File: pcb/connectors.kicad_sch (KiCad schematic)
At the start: 2 parts, among them J1 OBD2, J2 CAN

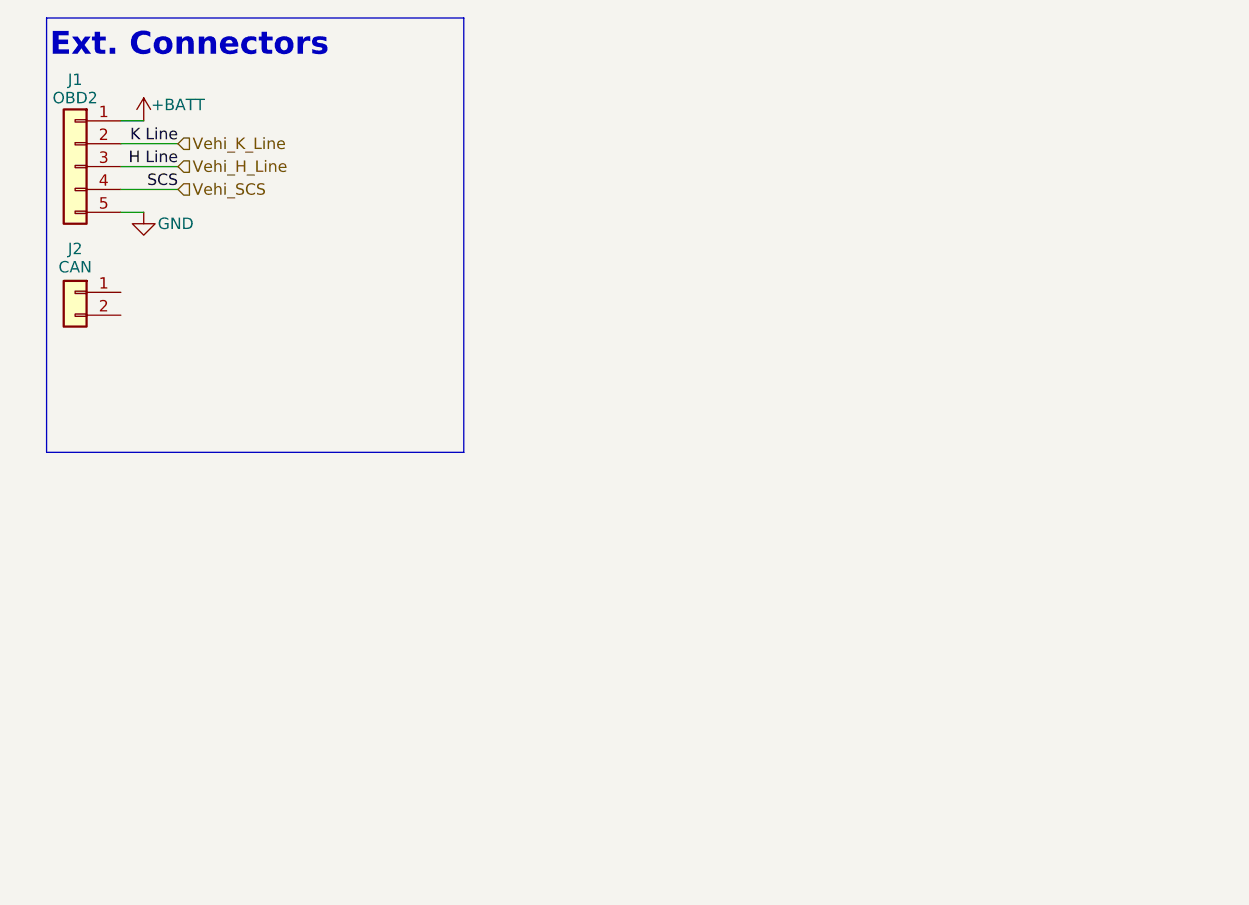
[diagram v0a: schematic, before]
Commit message: add transceivers, routing, drc
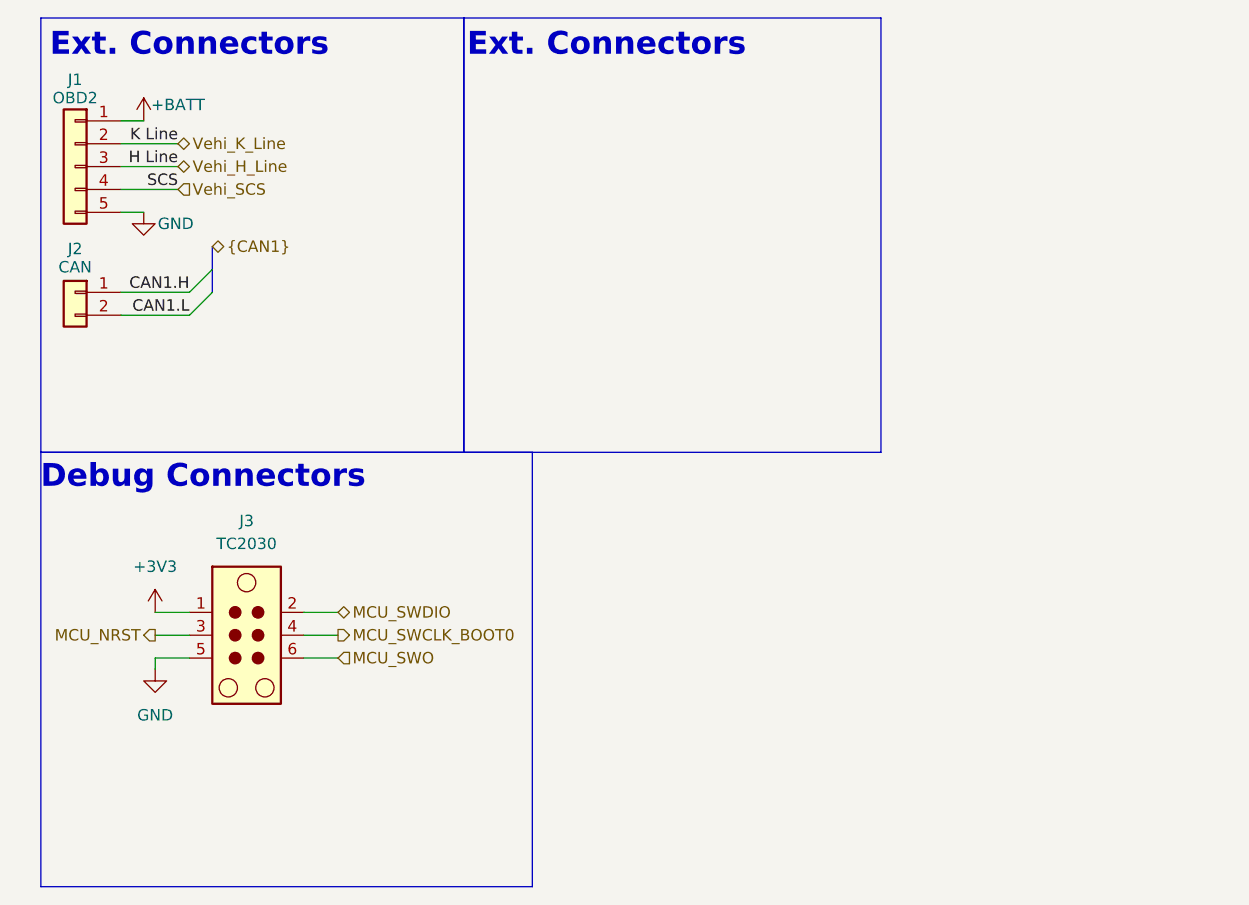
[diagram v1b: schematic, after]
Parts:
- added J3: TC2030, Connector:Tag-Connect_TC2030-IDC-NL_2x03_P1.27mm_Vertical, symbol Connector:TC2030
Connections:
- net GND: now also J3.5
- net CAN1.H: now reaches J2.1 (Pin_1)
- net CAN1.L: now reaches J2.2 (Pin_2)
- new net +3V3: J3.1
- new net MCU_NRST: J3.3
- new net MCU_SWCLK_BOOT0: J3.4
- new net MCU_SWDIO: J3.2
- new net MCU_SWO: J3.6
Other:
- note added: "Debug Connectors"

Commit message: busses are hard
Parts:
- added J3: USB-C 2.0, Connector_USB:USB_C_Receptacle_GCT_USB4105-xx-A_16P_TopMnt_Horizontal, symbol Connector:USB_C_Receptacle_USB2.0_16P
- added J4: RTC_BAT, Connector_Molex:Molex_PicoBlade_53047-0210_1x02_P1.25mm_Vertical, symbol Connector_Generic:Conn_01x02
- added R401, R402: 5.1k, Resistor_SMD:R_0402_1005Metric, symbol Device:R_Small
- renumbered J3 to J_SWD1
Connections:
- net GND: now also J3.A1 (GND), J3.A12 (GND), J3.B1 (GND), J3.B12 (GND), J3.S1 (SHIELD), J4.2 (Pin_2), R401.1, R402.2
- net CAN1.H renamed H_+
- net CAN1.L renamed L_-
- new net: J3.B5 (CC2), R402.1
- new net: J3.A5 (CC1), R401.2
- new net DN: J3.A7 (D-), J3.B7 (D-)
- new net DP: J3.A6 (D+), J3.B6 (D+)
- new net RTC_VBAT: J4.1 (Pin_1)
- new net USB_5V: J3.A4 (VBUS), J3.A9 (VBUS), J3.B4 (VBUS), J3.B9 (VBUS)
- no-connect marks 0 -> 2
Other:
- note added: "Int. Connectors"
- moved on the sheet: J1, J2, J_SWD1

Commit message: CAN/mcu placement/routing
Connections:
- net H_+ renamed CAN.P
- net L_- renamed CAN.N
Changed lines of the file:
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@@
 		)
 	)
-	(label "H_+"
+	(label "CAN.P"
 		(at 27.94 50.8 0)
 		(effects
@@
 		)
 	)
-	(label "L_-"
+	(label "CAN.N"
 		(at 27.94 53.34 0)
 		(effects
@@
 		)
 	)
-	(hierarchical_label "{CAN}"
+	(hierarchical_label "CAN{CAN}"
 		(shape bidirectional)
 		(at 36.83 45.72 180)

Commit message: fix CAN tx/rx/stb, remove unused SWO
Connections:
- net MCU_SWO: no longer names the net of J_SWD1.6
- no-connect marks 2 -> 3
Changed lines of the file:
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@@
 		(at 74.93 53.34)
+	)
+	(no_connect
+		(at 44.45 87.63)
 	)
 	(bus_entry
@@
 	(wire
 		(pts
-			(xy 44.45 87.63) (xy 48.26 87.63)
-		)
-		(stroke
-			(width 0)
-			(type default)
-		)
-	)
-	(wire
-		(pts
 			(xy 74.93 35.56) (xy 76.2 35.56)
 		)
@@
 		(effects
 			(font
-				(size 1.27 1.27)
-			)
-			(justify left)
-		)
-	)
-	(hierarchical_label "MCU_SWO"
-		(shape input)
-		(at 48.26 87.63 0)
-		(effects
-			(font

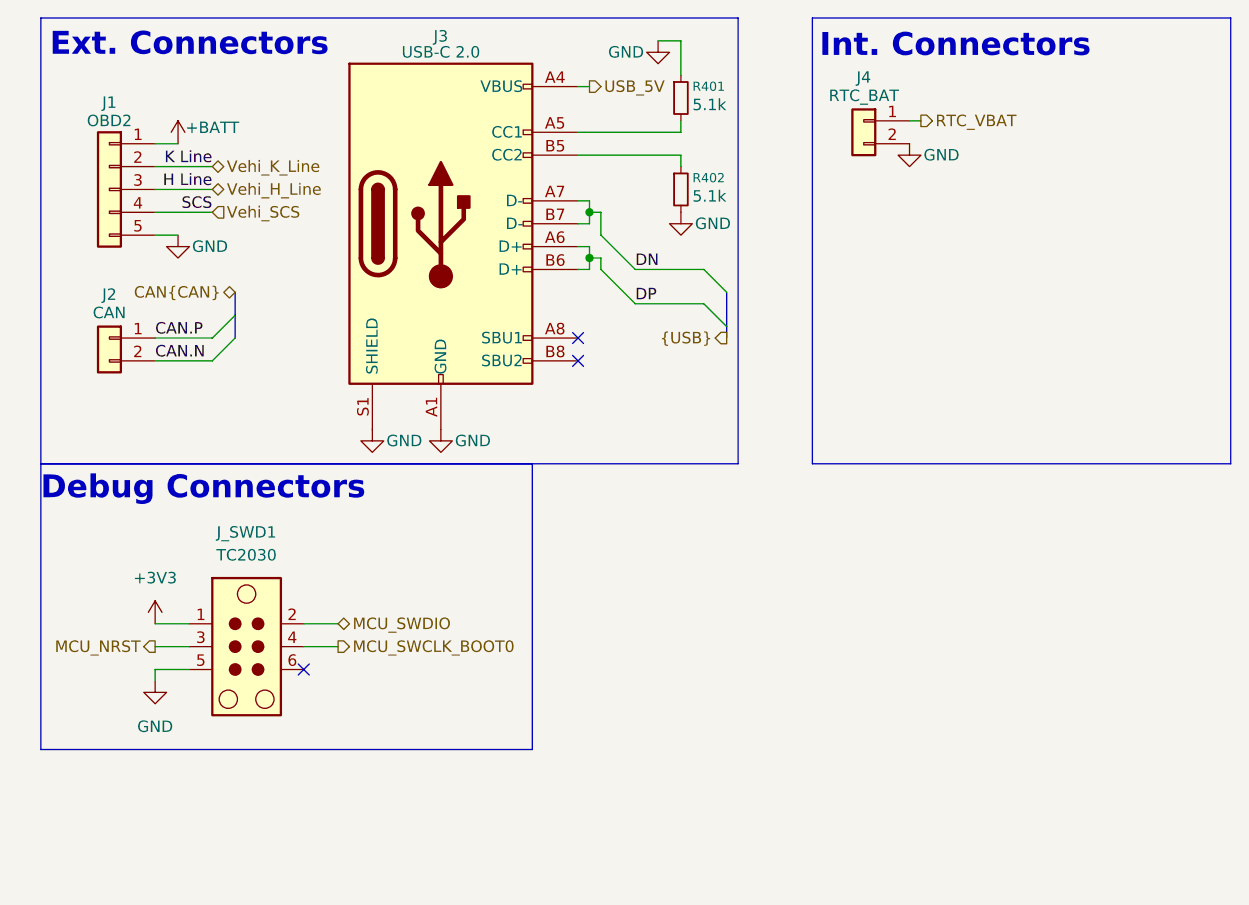
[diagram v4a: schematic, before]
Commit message: status/info leds, extra 5v cap
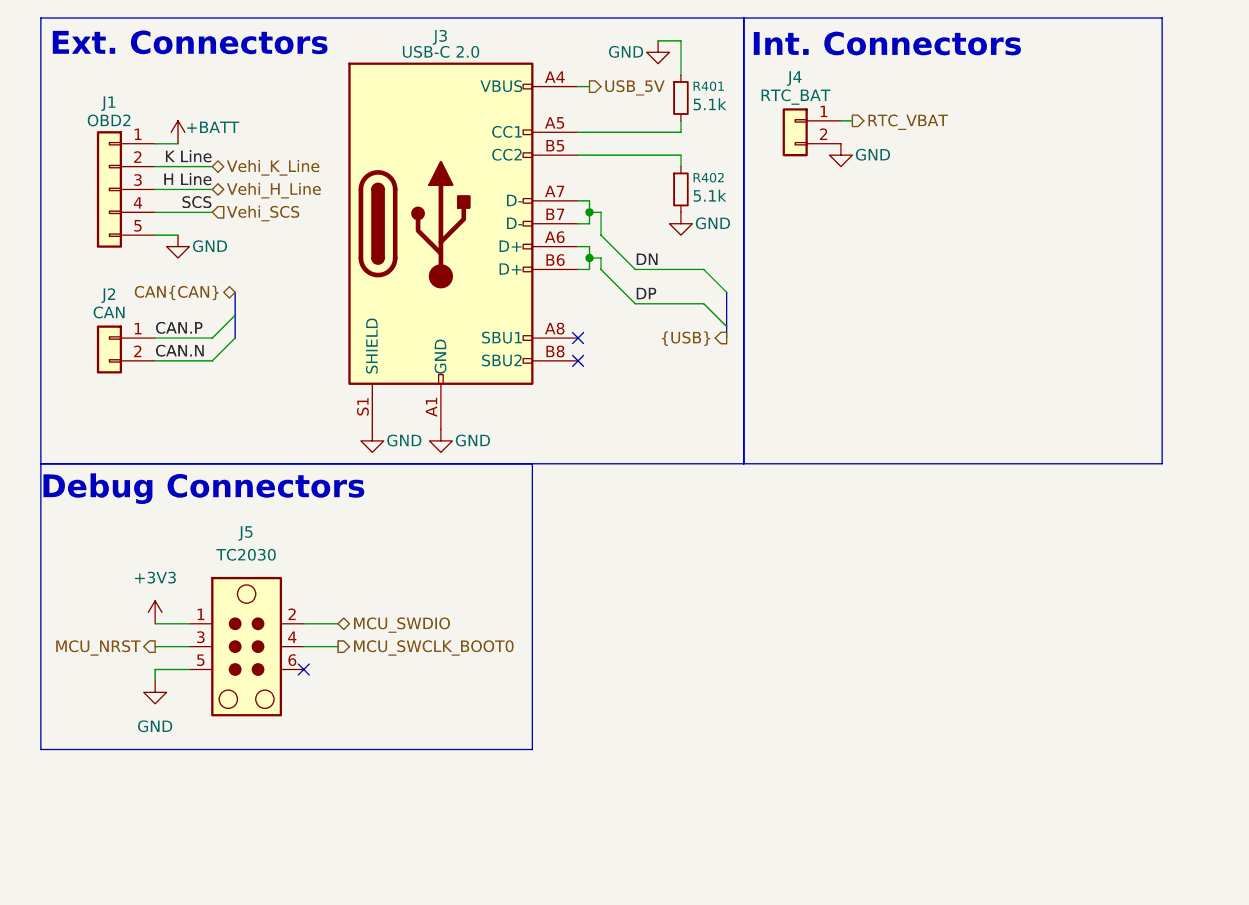
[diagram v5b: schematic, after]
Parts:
- renumbered J_SWD1 to J5
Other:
- moved on the sheet: J4
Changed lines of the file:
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@@
 	(rectangle
 		(start 15.24 15.24)
-		(end 92.71 64.77)
+		(end 93.345 64.77)
 		(stroke
 			(width 0)
@@
 	)
 	(rectangle
-		(start 100.965 15.24)
-		(end 147.447 64.77)
+		(start 93.345 15.24)
+		(end 139.827 64.77)
 		(stroke
 			(width 0)
@@
 	(text "Int. Connectors"
 		(exclude_from_sim no)
-		(at 116.84 18.415 0)
+		(at 109.22 18.415 0)
 		(effects
 			(font
@@
 	(wire
 		(pts
-			(xy 111.76 26.67) (xy 113.03 26.67)
+			(xy 104.14 26.67) (xy 105.41 26.67)
 		)
 		(stroke
@@
 	(hierarchical_label "RTC_VBAT"
 		(shape output)
-		(at 113.03 26.67 0)
+		(at 105.41 26.67 0)
 		(effects
 			(font
@@
 	(symbol
 		(lib_id "power:GND")
-		(at 111.76 29.21 0)
+		(at 104.14 29.21 0)
 		(unit 1)
 		(exclude_from_sim no)
@@
 		(dnp no)
 		(property "Reference" "#PWR037"
-			(at 111.76 35.56 0)
+			(at 104.14 35.56 0)
 			(effects
 				(font
@@
 		)
 		(property "Value" "GND"
-			(at 115.316 30.48 0)
+			(at 107.696 30.48 0)
 			(effects
 				(font
@@
 		)
 		(property "Footprint" ""
-			(at 111.76 29.21 0)
+			(at 104.14 29.21 0)
 			(effects
 				(font
@@
 		)
 		(property "Datasheet" ""
-			(at 111.76 29.21 0)
+			(at 104.14 29.21 0)
 			(effects
 				(font
@@
 		)
 		(property "Description" "Power symbol creates a global label with name \"GND\" , ground"
-			(at 111.76 29.21 0)
+			(at 104.14 29.21 0)
 			(effects
 				(font
@@
 		(dnp no)
 		(fields_autoplaced yes)
-		(property "Reference" "J_SWD1"
+		(property "Reference" "J5"
 			(at 38.1 72.39 0)
 			(effects
@@
 			(project ""
 				(path "/0736e313-8db4-41af-b70d-53af7104d2ca/327da5f9-d937-42ff-b3b7-f3be294fa76c"
-					(reference "J_SWD1")
+					(reference "J5")
 					(unit 1)
 				)
@@
 	(symbol
 		(lib_id "Connector_Generic:Conn_01x02")
-		(at 106.68 26.67 0)
+		(at 99.06 26.67 0)
 		(mirror y)
 		(unit 1)
@@
 		(dnp no)
 		(property "Reference" "J4"
-			(at 106.68 21.844 0)
+			(at 99.06 21.844 0)
 			(effects
 				(font
@@
 		)
 		(property "Value" "RTC_BAT"
-			(at 106.68 23.876 0)
+			(at 99.06 23.876 0)
 			(effects
 				(font
@@
 		)
 		(property "Footprint" "Connector_Molex:Molex_PicoBlade_53047-0210_1x02_P1.25mm_Vertical"
-			(at 106.68 26.67 0)
+			(at 99.06 26.67 0)
 			(effects
 				(font
@@
 		)
 		(property "Datasheet" "~"
-			(at 106.68 26.67 0)
+			(at 99.06 26.67 0)
 			(effects
 				(font
@@
 		)
 		(property "Description" "Generic connector, single row, 01x02, script generated (kicad-library-utils/schlib/autogen/connector/)"
-			(at 106.68 26.67 0)
-			(effects
-				(font
+			(at 99.06 26.67 0)
+			(effects
+				(font

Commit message: dbg uart, nrst, SCS drive, etc
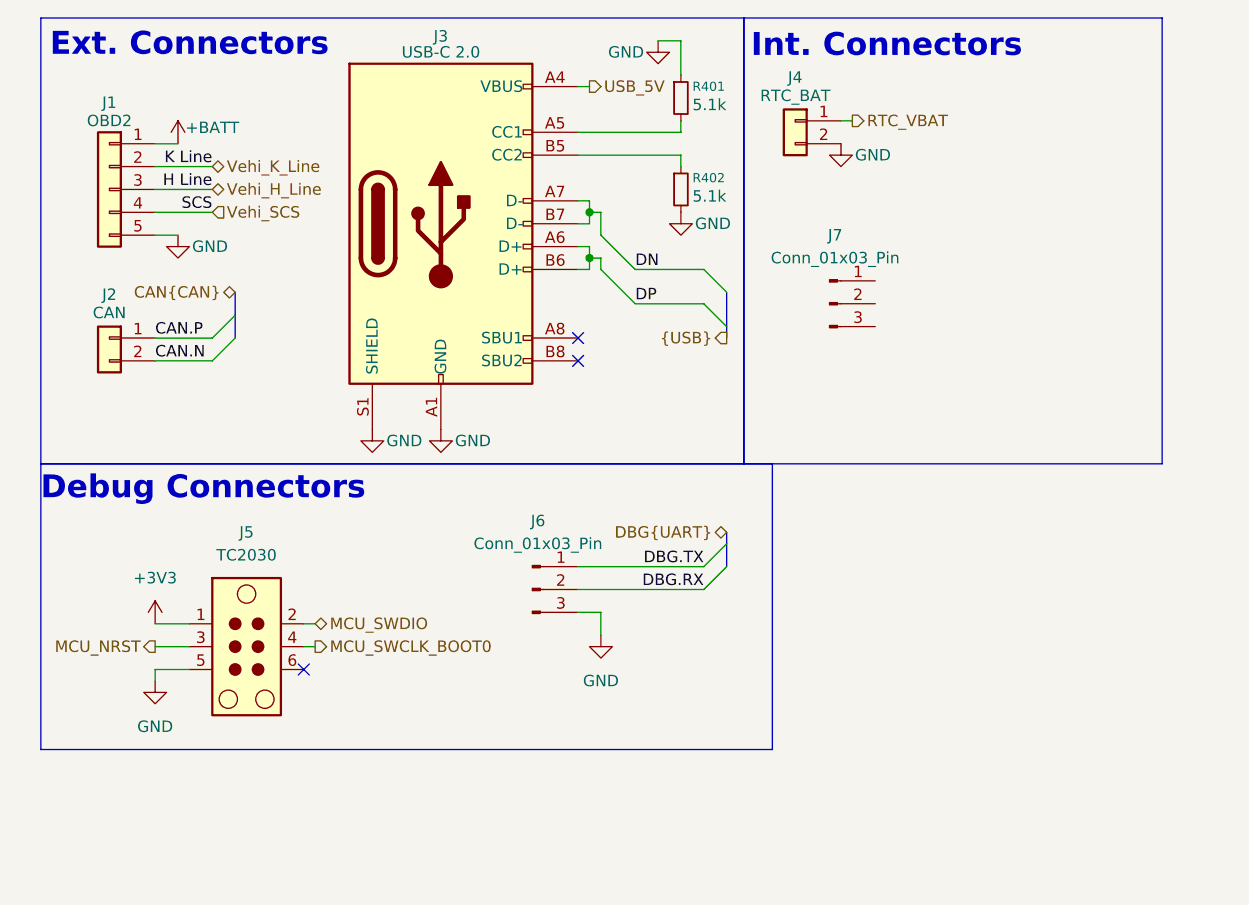
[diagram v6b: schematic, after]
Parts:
- added J6, J7: Conn_01x03_Pin, Connector_PinHeader_2.54mm:PinHeader_1x03_P2.54mm_Vertical_SMD_Pin1Left, symbol Connector:Conn_01x03_Pin
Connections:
- net GND: now also J6.3 (Pin_3)
- new net DBG.RX: J6.2 (Pin_2)
- new net DBG.TX: J6.1 (Pin_1)

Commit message: connector prep
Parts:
- removed J7: Conn_01x03_Pin, Connector_PinHeader_2.54mm:PinHeader_1x03_P2.54mm_Vertical_SMD_Pin1Left, symbol Connector:Conn_01x03_Pin
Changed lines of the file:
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@@
-	)
-	(symbol
-		(lib_id "Connector:Conn_01x03_Pin")
-		(at 102.87 46.99 0)
-		(unit 1)
-		(exclude_from_sim no)
-		(in_bom yes)
-		(on_board yes)
-		(dnp no)
-		(fields_autoplaced yes)
-		(property "Reference" "J7"
-			(at 103.505 39.37 0)
-			(effects
-				(font
-					(size 1.27 1.27)
-				)
-			)
-		)
-		(property "Value" "Conn_01x03_Pin"
-			(at 103.505 41.91 0)
-			(effects
-				(font
-					(size 1.27 1.27)
-				)
-			)
-		)
-		(property "Footprint" "Connector_PinHeader_2.54mm:PinHeader_1x03_P2.54mm_Vertical_SMD_Pin1Left"
-			(at 102.87 46.99 0)
-			(effects
-				(font
-					(size 1.27 1.27)
-				)
-				(hide yes)
-			)
-		)
-		(property "Datasheet" "~"
-			(at 102.87 46.99 0)
-			(effects
-				(font
-					(size 1.27 1.27)
-				)
-				(hide yes)
-			)
-		)
-		(property "Description" "Generic connector, single row, 01x03, script generated"
-			(at 102.87 46.99 0)
-			(effects
-				(font
-					(size 1.27 1.27)
-				)
-				(hide yes)
-			)
-		)
-		(pin "2"
-		)
-		(pin "3"
-		)
-		(pin "1"
-		)
-		(instances
-			(project "kh_obd2_interface"
-				(path "/0736e313-8db4-41af-b70d-53af7104d2ca/327da5f9-d937-42ff-b3b7-f3be294fa76c"
-					(reference "J7")
-					(unit 1)
-				)
-			)
-		)
 	)
 	(symbol
